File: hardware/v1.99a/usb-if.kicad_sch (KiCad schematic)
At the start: 25 parts, among them J1 USB_C_Receptacle_USB2.0, J2 Conn_02x05_Odd_Even, U1 TPD3S014, U4 CH32V307VCT6, Y1 24M

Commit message: v1.99a: Move FGPA_CLK to MCO pin.
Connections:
- net FTDI_CLK: now also U4.67 (PA8); no longer U4.47 (PB10)
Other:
- note added: "MCO/TIM1_CH1"
- note removed: "TIM2_CH3"
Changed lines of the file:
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@@
+    (stroke (width 0) (type default) (color 0 0 0 0))
+  )
+  (wire (pts (xy 109.22 60.96) (xy 110.49 60.96))
     (stroke (width 0) (type default) (color 0 0 0 0))
   )
@@
     (stroke (width 0) (type default) (color 0 0 0 0))
   )
-  (wire (pts (xy 109.22 109.22) (xy 110.49 109.22))
-    (stroke (width 0) (type default) (color 0 0 0 0))
-  )
   (wire (pts (xy 60.96 40.64) (xy 54.61 40.64))
     (stroke (width 0) (type default) (color 0 0 0 0))
@@
     (effects (font (size 1.27 1.27)) (justify right bottom))
   )
+  (text "MCO/TIM1_CH1" (at 92.71 62.23 180)
+    (effects (font (size 1.27 1.27)) (justify right bottom))
+  )
   (text "SPI1_SCK\n" (at 87.63 54.61 180)
     (effects (font (size 1.27 1.27)) (justify right bottom))
@@
     (effects (font (size 1.27 1.27)) (justify right bottom))
   )
-  (text "TIM2_CH3" (at 96.52 110.49 180)
-    (effects (font (size 1.27 1.27)) (justify right bottom))
-  )
   (text "SDIO_CMD\n" (at 69.85 133.35 0)
     (effects (font (size 1.27 1.27)) (justify left bottom))
@@
     )
   )
-  (global_label "FTDI_CLK" (shape input) (at 110.49 109.22 0) (fields_autoplaced)
-    (effects (font (size 1.27 1.27)) (justify left))
-    (property "Intersheet References" "${INTERSHEET_REFS}" (id 0) (at 121.2809 109.1406 0)
-      (effects (font (size 1.27 1.27)) (justify left) hide)
-    )
-  )
   (global_label "FLASH_MOSI|IO0" (shape input) (at 110.49 58.42 0) (fields_autoplaced)
     (effects (font (size 1.27 1.27)) (justify left))
@@
       (effects (font (size 1.27 1.27)) (justify left) hide)
     )
+  )
+  (global_label "FTDI_CLK" (shape input) (at 110.49 60.96 0) (fields_autoplaced)
+    (effects (font (size 1.27 1.27)) (justify left))
+    (property "Intersheet References" "${INTERSHEET_REFS}" (id 0) (at 121.2809 60.8806 0)
+      (effects (font (size 1.27 1.27)) (justify left) hide)
+    )

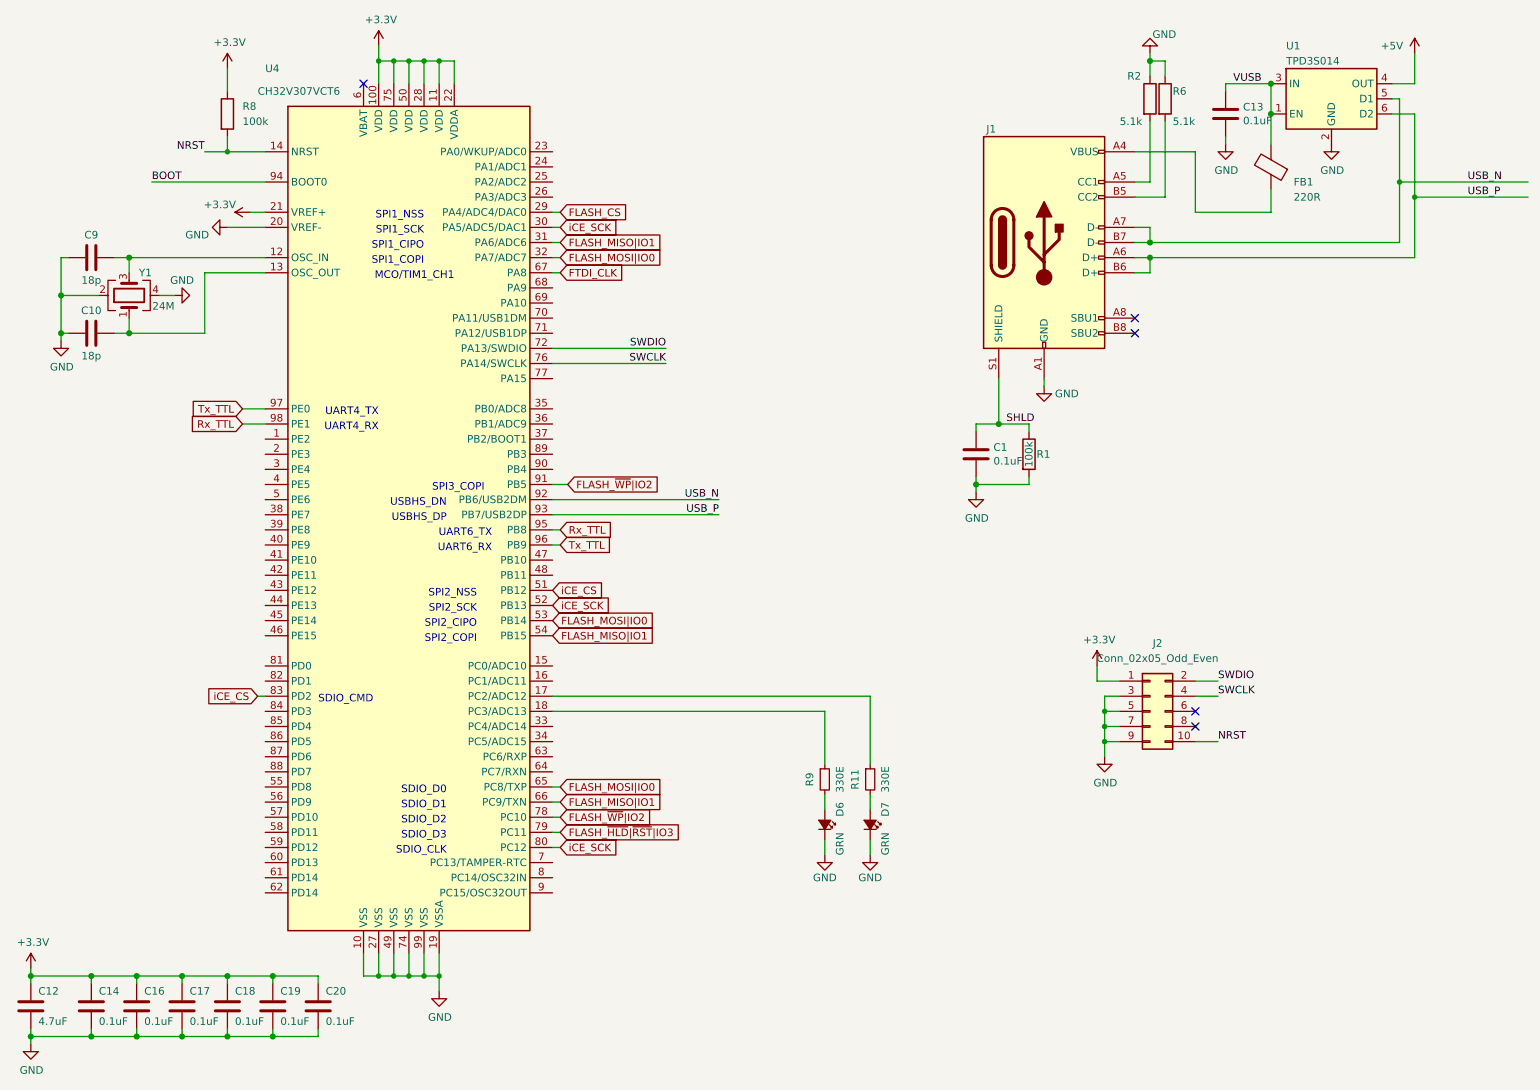
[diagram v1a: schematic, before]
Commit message: v1.99a: Update
- Rename nets
- Add Debug UART channel to 10P SWD connector
- Add analog mux default on for iCE_CS/FLASH_CS
- Connect DONE/RESET
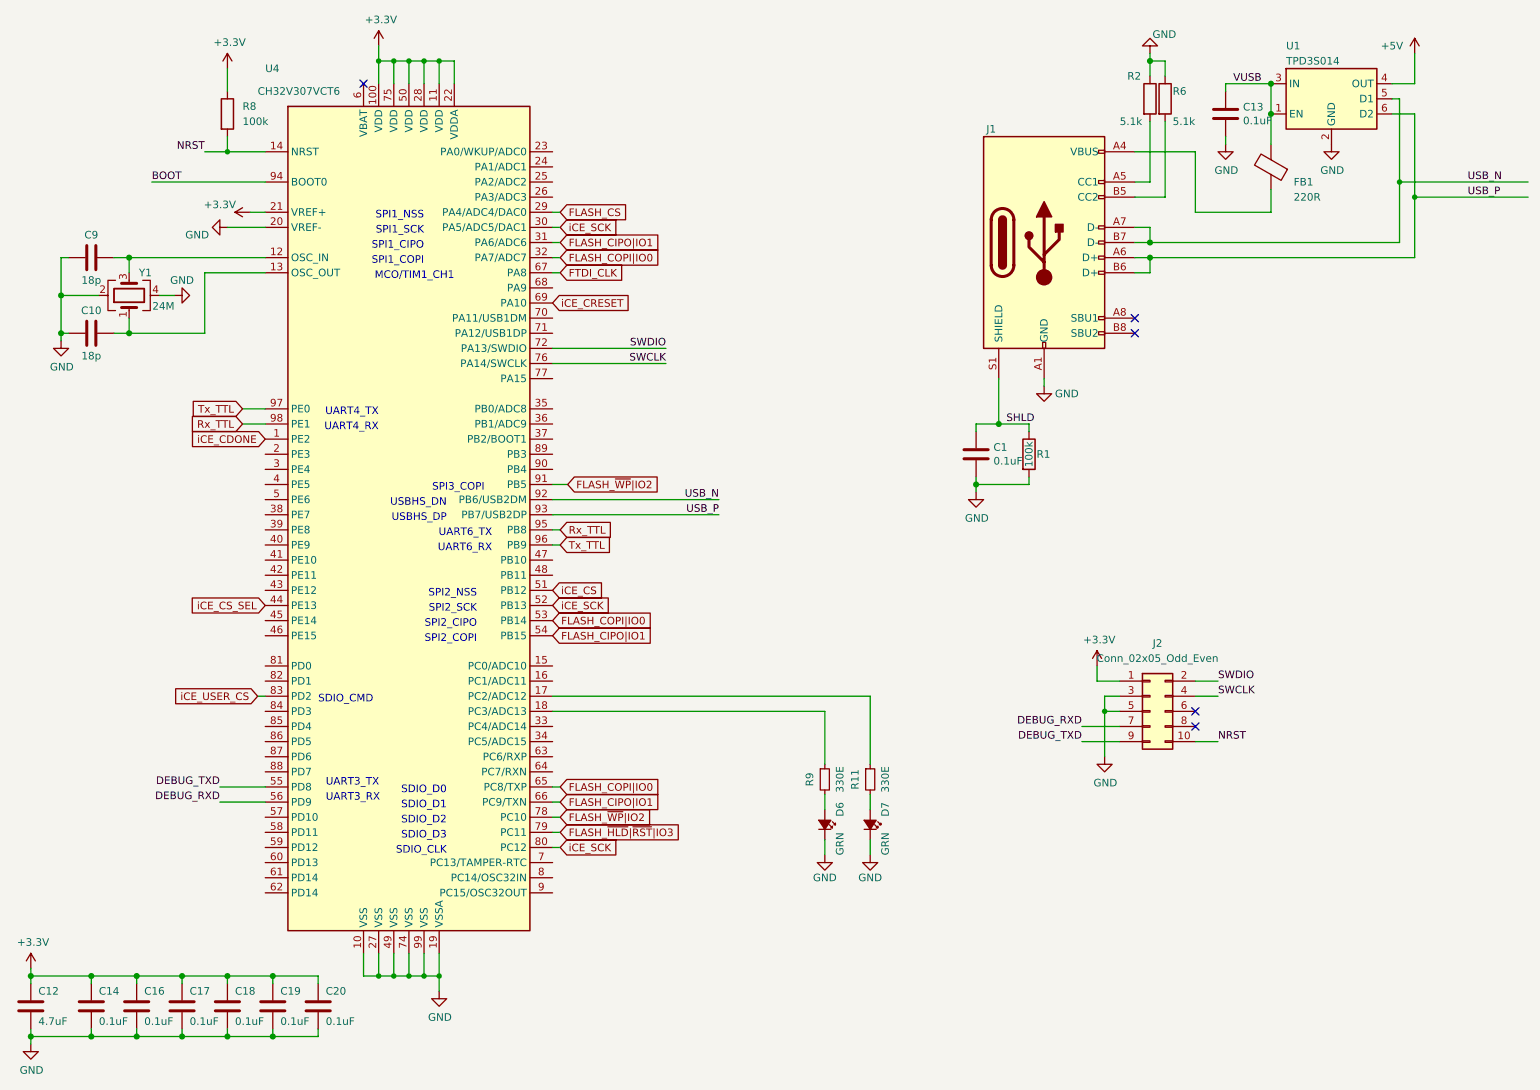
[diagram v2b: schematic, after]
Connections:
- net GND: no longer J2.7 (Pin_7), J2.9 (Pin_9)
- net iCE_CS: no longer U4.83 (PD2)
- net iCE_CDONE: now reaches U4.1 (PE2)
- net iCE_CS_SEL: now reaches U4.44 (PE13)
- net DEBUG_TXD: now reaches U4.55 (PD8)
- net DEBUG_TXD: now also J2.9 (Pin_9)
- net DEBUG_RXD: now reaches U4.56 (PD9)
- net DEBUG_RXD: now also J2.7 (Pin_7)
- net iCE_CRESET: now reaches U4.69 (PA10)
- net FLASH_MISO|IO1 renamed FLASH_CIPO|IO1
- net FLASH_MOSI|IO0 renamed FLASH_COPI|IO0
- new net iCE_USER_CS: U4.83 (PD2)
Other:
- note added: "UART3_RX"
- note added: "UART3_TX"
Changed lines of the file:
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@@
   (junction (at 26.67 71.12) (diameter 1.016) (color 0 0 0 0)
   )
-  (junction (at 201.93 137.16) (diameter 0) (color 0 0 0 0)
-  )
   (junction (at 54.61 179.07) (diameter 1.016) (color 0 0 0 0)
   )
@@
   )
   (junction (at 54.61 40.64) (diameter 0) (color 0 0 0 0)
-  )
-  (junction (at 201.93 139.7) (diameter 0) (color 0 0 0 0)
   )
   (junction (at 39.37 179.07) (diameter 1.016) (color 0 0 0 0)
@@
     (stroke (width 0) (type default) (color 0 0 0 0))
   )
-  (wire (pts (xy 201.93 139.7) (xy 204.47 139.7))
-    (stroke (width 0) (type default) (color 0 0 0 0))
-  )
   (wire (pts (xy 62.23 187.96) (xy 62.23 189.23))
     (stroke (width 0) (type solid) (color 0 0 0 0))
@@
     (stroke (width 0) (type solid) (color 0 0 0 0))
   )
-  (wire (pts (xy 201.93 139.7) (xy 201.93 142.24))
-    (stroke (width 0) (type default) (color 0 0 0 0))
-  )
   (wire (pts (xy 209.55 55.88) (xy 251.46 55.88))
     (stroke (width 0) (type solid) (color 0 0 0 0))
@@
     (stroke (width 0) (type solid) (color 0 0 0 0))
   )
+  (wire (pts (xy 53.34 147.32) (xy 60.96 147.32))
+    (stroke (width 0) (type default) (color 0 0 0 0))
+  )
   (wire (pts (xy 54.61 179.07) (xy 54.61 180.34))
     (stroke (width 0) (type solid) (color 0 0 0 0))
@@
     (stroke (width 0) (type solid) (color 0 0 0 0))
   )
-  (wire (pts (xy 201.93 137.16) (xy 204.47 137.16))
-    (stroke (width 0) (type default) (color 0 0 0 0))
-  )
   (wire (pts (xy 209.55 35.56) (xy 209.55 45.72))
     (stroke (width 0) (type solid) (color 0 0 0 0))
@@
     (stroke (width 0) (type default) (color 0 0 0 0))
   )
-  (wire (pts (xy 201.93 134.62) (xy 201.93 137.16))
+  (wire (pts (xy 201.93 134.62) (xy 201.93 142.24))
     (stroke (width 0) (type default) (color 0 0 0 0))
   )
@@
     (stroke (width 0) (type solid) (color 0 0 0 0))
   )
+  (wire (pts (xy 53.34 149.86) (xy 60.96 149.86))
+    (stroke (width 0) (type default) (color 0 0 0 0))
+  )
   (wire (pts (xy 21.59 190.5) (xy 21.59 189.23))
     (stroke (width 0) (type solid) (color 0 0 0 0))
@@
     (stroke (width 0) (type solid) (color 0 0 0 0))
   )
+  (wire (pts (xy 198.12 139.7) (xy 204.47 139.7))
+    (stroke (width 0) (type default) (color 0 0 0 0))
+  )
   (wire (pts (xy 57.15 83.82) (xy 60.96 83.82))
     (stroke (width 0) (type default) (color 0 0 0 0))
   )
+  (wire (pts (xy 198.12 137.16) (xy 204.47 137.16))
+    (stroke (width 0) (type default) (color 0 0 0 0))
+  )
   (wire (pts (xy 60.96 40.64) (xy 54.61 40.64))
     (stroke (width 0) (type default) (color 0 0 0 0))
@@
     (stroke (width 0) (type default) (color 0 0 0 0))
   )
-  (wire (pts (xy 201.93 137.16) (xy 201.93 139.7))
-    (stroke (width 0) (type default) (color 0 0 0 0))
-  )
   (wire (pts (xy 217.17 129.54) (xy 220.98 129.54))
     (stroke (width 0) (type default) (color 0 0 0 0))
@@
     (effects (font (size 1.27 1.27)) (justify right bottom))
   )
+  (text "UART3_RX\n" (at 71.12 149.86 0)
+    (effects (font (size 1.27 1.27)) (justify left bottom))
+  )
   (text "UART4_TX" (at 80.01 85.09 180)
     (effects (font (size 1.27 1.27)) (justify right bottom))
@@
     (effects (font (size 1.27 1.27)) (justify right bottom))
   )
+  (text "UART3_TX" (at 71.12 147.32 0)
+    (effects (font (size 1.27 1.27)) (justify left bottom))
+  )
   (text "SPI1_SCK\n" (at 87.63 54.61 180)
     (effects (font (size 1.27 1.27)) (justify right bottom))
@@
     (effects (font (size 1.27 1.27)) (justify right bottom))
   )
+  (label "DEBUG_RXD" (at 53.34 149.86 180)
+    (effects (font (size 1.27 1.27)) (justify right bottom))
+  )
   (label "SWDIO" (at 128.27 73.66 180)
     (effects (font (size 1.27 1.27)) (justify right bottom))
@@
     (effects (font (size 1.27 1.27)) (justify left bottom))
   )
+  (label "DEBUG_TXD" (at 198.12 139.7 180)
+    (effects (font (size 1.27 1.27)) (justify right bottom))
+  )
   (label "USB_N" (at 137.16 99.06 180)
     (effects (font (size 1.27 1.27)) (justify right bottom))
   )
+  (label "DEBUG_TXD" (at 53.34 147.32 180)
+    (effects (font (size 1.27 1.27)) (justify right bottom))
+  )
   (label "USB_P" (at 137.16 101.6 180)
     (effects (font (size 1.27 1.27)) (justify right bottom))
@@
     (effects (font (size 1.27 1.27)) (justify right bottom))
   )
+  (label "DEBUG_RXD" (at 198.12 137.16 180)
+    (effects (font (size 1.27 1.27)) (justify right bottom))
+  )
   (global_label "Tx_TTL" (shape input) (at 110.49 106.68 0) (fields_autoplaced)
     (effects (font (size 1.27 1.27)) (justify left))
@@
     )
   )
-  (global_label "FLASH_MOSI|IO0" (shape input) (at 110.49 58.42 0) (fields_autoplaced)
-    (effects (font (size 1.27 1.27)) (justify left))
-    (property "Intersheet References" "${INTERSHEET_REFS}" (id 0) (at 128.4775 58.3406 0)
+  (global_label "iCE_USER_CS" (shape input) (at 59.69 132.08 180) (fields_autoplaced)
+    (effects (font (size 1.27 1.27)) (justify right))
+    (property "Intersheet References" "${INTERSHEET_REFS}" (id 0) (at 44.9682 132.1594 0)
+      (effects (font (size 1.27 1.27)) (justify right) hide)
+    )
+  )
+  (global_label "iCE_CDONE" (shape input) (at 60.96 88.9 180) (fields_autoplaced)
+    (effects (font (size 1.27 1.27)) (justify right))
+    (property "Intersheet References" "${INTERSHEET_REFS}" (id 0) (at 48.2944 88.9794 0)
+      (effects (font (size 1.27 1.27)) (justify right) hide)
+    )
+  )
+  (global_label "FLASH_COPI|IO0" (shape input) (at 110.49 58.42 0) (fields_autoplaced)
+    (effects (font (size 1.27 1.27)) (justify left))
+    (property "Intersheet References" "${INTERSHEET_REFS}" (id 0) (at 128.3566 58.3406 0)
       (effects (font (size 1.27 1.27)) (justify left) hide)
     )
@@
     )
   )
-  (global_label "FLASH_MOSI|IO0" (shape input) (at 109.22 119.38 0) (fields_autoplaced)
-    (effects (font (size 1.27 1.27)) (justify left))
-    (property "Intersheet References" "${INTERSHEET_REFS}" (id 0) (at 127.2075 119.3006 0)
+  (global_label "iCE_CS_SEL" (shape input) (at 60.96 116.84 180) (fields_autoplaced)
+    (effects (font (size 1.27 1.27)) (justify right))
+    (property "Intersheet References" "${INTERSHEET_REFS}" (id 0) (at 47.8106 116.7606 0)
+      (effects (font (size 1.27 1.27)) (justify right) hide)
+    )
+  )
+  (global_label "iCE_CRESET" (shape input) (at 109.22 66.04 0) (fields_autoplaced)
+    (effects (font (size 1.27 1.27)) (justify left))
+    (property "Intersheet References" "${INTERSHEET_REFS}" (id 0) (at 122.5509 65.9606 0)
+      (effects (font (size 1.27 1.27)) (justify left) hide)
+    )
+  )
+  (global_label "FLASH_COPI|IO0" (shape input) (at 109.22 119.38 0) (fields_autoplaced)
+    (effects (font (size 1.27 1.27)) (justify left))
+    (property "Intersheet References" "${INTERSHEET_REFS}" (id 0) (at 127.0866 119.3006 0)
       (effects (font (size 1.27 1.27)) (justify left) hide)
     )
@@
     )
   )
-  (global_label "FLASH_MISO|IO1" (shape input) (at 110.49 149.86 0) (fields_autoplaced)
-    (effects (font (size 1.27 1.27)) (justify left))
-    (property "Intersheet References" "${INTERSHEET_REFS}" (id 0) (at 128.4775 149.7806 0)
-      (effects (font (size 1.27 1.27)) (justify left) hide)
-    )
-  )
-  (global_label "iCE_CS" (shape input) (at 59.69 132.08 180) (fields_autoplaced)
-    (effects (font (size 1.27 1.27)) (justify right))
-    (property "Intersheet References" "${INTERSHEET_REFS}" (id 0) (at 50.8948 132.1594 0)
-      (effects (font (size 1.27 1.27)) (justify right) hide)
-    )
-  )
-  (global_label "FLASH_MOSI|IO0" (shape input) (at 110.49 147.32 0) (fields_autoplaced)
-    (effects (font (size 1.27 1.27)) (justify left))
-    (property "Intersheet References" "${INTERSHEET_REFS}" (id 0) (at 128.4775 147.2406 0)
+  (global_label "FLASH_CIPO|IO1" (shape input) (at 110.49 149.86 0) (fields_autoplaced)
+    (effects (font (size 1.27 1.27)) (justify left))
+    (property "Intersheet References" "${INTERSHEET_REFS}" (id 0) (at 128.3566 149.7806 0)
+      (effects (font (size 1.27 1.27)) (justify left) hide)
+    )
+  )
+  (global_label "FLASH_COPI|IO0" (shape input) (at 110.49 147.32 0) (fields_autoplaced)
+    (effects (font (size 1.27 1.27)) (justify left))
+    (property "Intersheet References" "${INTERSHEET_REFS}" (id 0) (at 128.3566 147.2406 0)
       (effects (font (size 1.27 1.27)) (justify left) hide)
     )
@@
     )
   )
-  (global_label "FLASH_MISO|IO1" (shape input) (at 109.22 121.92 0) (fields_autoplaced)
-    (effects (font (size 1.27 1.27)) (justify left))
-    (property "Intersheet References" "${INTERSHEET_REFS}" (id 0) (at 127.2075 121.8406 0)
+  (global_label "FLASH_CIPO|IO1" (shape input) (at 109.22 121.92 0) (fields_autoplaced)
+    (effects (font (size 1.27 1.27)) (justify left))
+    (property "Intersheet References" "${INTERSHEET_REFS}" (id 0) (at 127.0866 121.8406 0)
       (effects (font (size 1.27 1.27)) (justify left) hide)
     )
@@
     )
   )
-  (global_label "FLASH_MISO|IO1" (shape input) (at 110.49 55.88 0) (fields_autoplaced)
-    (effects (font (size 1.27 1.27)) (justify left))
-    (property "Intersheet References" "${INTERSHEET_REFS}" (id 0) (at 128.4775 55.8006 0)
-      (effects (font (size 1.27 1.27)) (justify left) hide)
-    )
+  (global_label "FLASH_CIPO|IO1" (shape input) (at 110.49 55.88 0) (fields_autoplaced)
+    (effects (font (size 1.27 1.27)) (justify left))
+    (property "Intersheet References" "${INTERSHEET_REFS}" (id 0) (at 128.3566 55.8006 0)
+      (effects (font (size 1.27 1.27)) (justify left) hide)
+    )

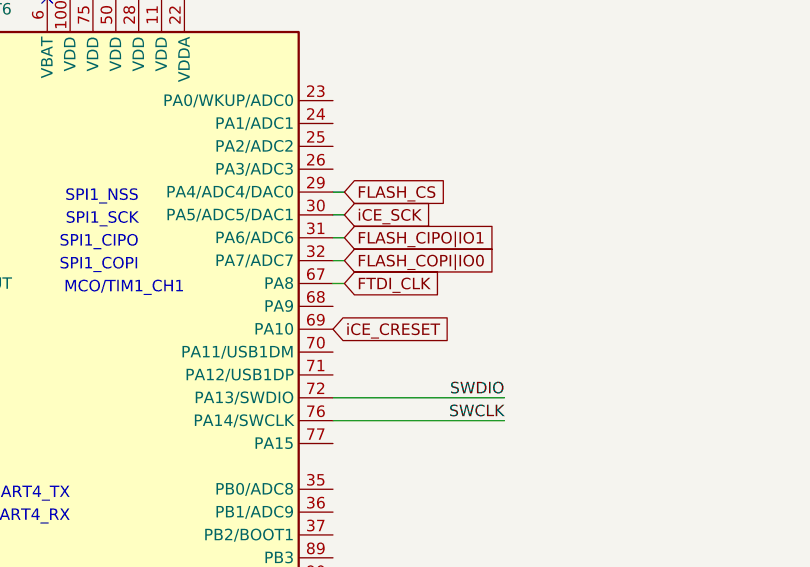
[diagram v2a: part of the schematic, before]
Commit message: Rename FTDI_CLK to FPGA_CLK.
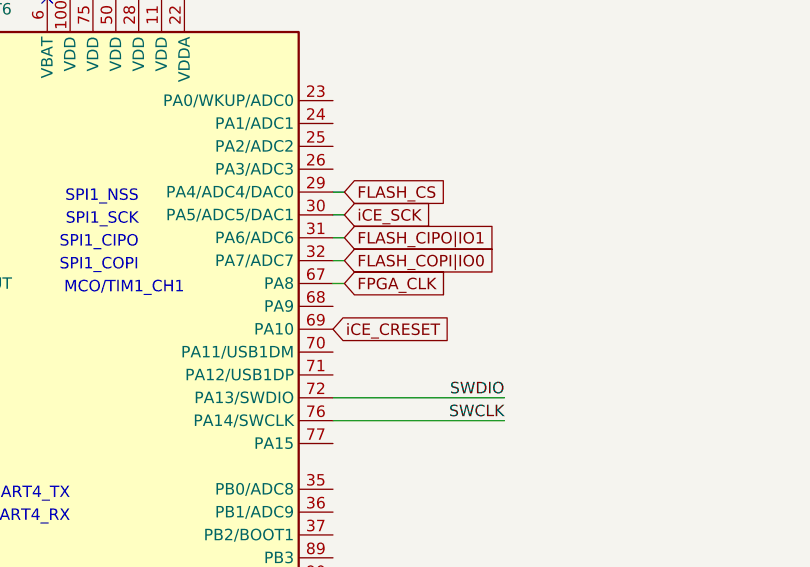
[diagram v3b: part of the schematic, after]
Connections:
- net FTDI_CLK renamed FPGA_CLK
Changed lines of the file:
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@@
     )
   )
-  (global_label "FTDI_CLK" (shape input) (at 110.49 60.96 0) (fields_autoplaced)
+  (global_label "FPGA_CLK" (shape input) (at 110.49 60.96 0) (fields_autoplaced)
     (effects (font (size 1.27 1.27)) (justify left))
-    (property "Intersheet References" "${INTERSHEET_REFS}" (id 0) (at 121.2809 60.8806 0)
+    (property "Intersheet References" "${INTERSHEET_REFS}" (id 0) (at 122.0671 60.8806 0)
       (effects (font (size 1.27 1.27)) (justify left) hide)
     )
